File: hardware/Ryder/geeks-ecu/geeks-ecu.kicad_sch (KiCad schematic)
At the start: 25 parts, among them J101 7.62mm, J102 5.08mm, J103 JST XH, J104 5.08mm, J105 5.08mm, J106 5.08mm, J107 5.08mm, J108 5.08mm, J109 5.08mm, J110 5.08mm, J111 5.08mm, K101 J115F11A

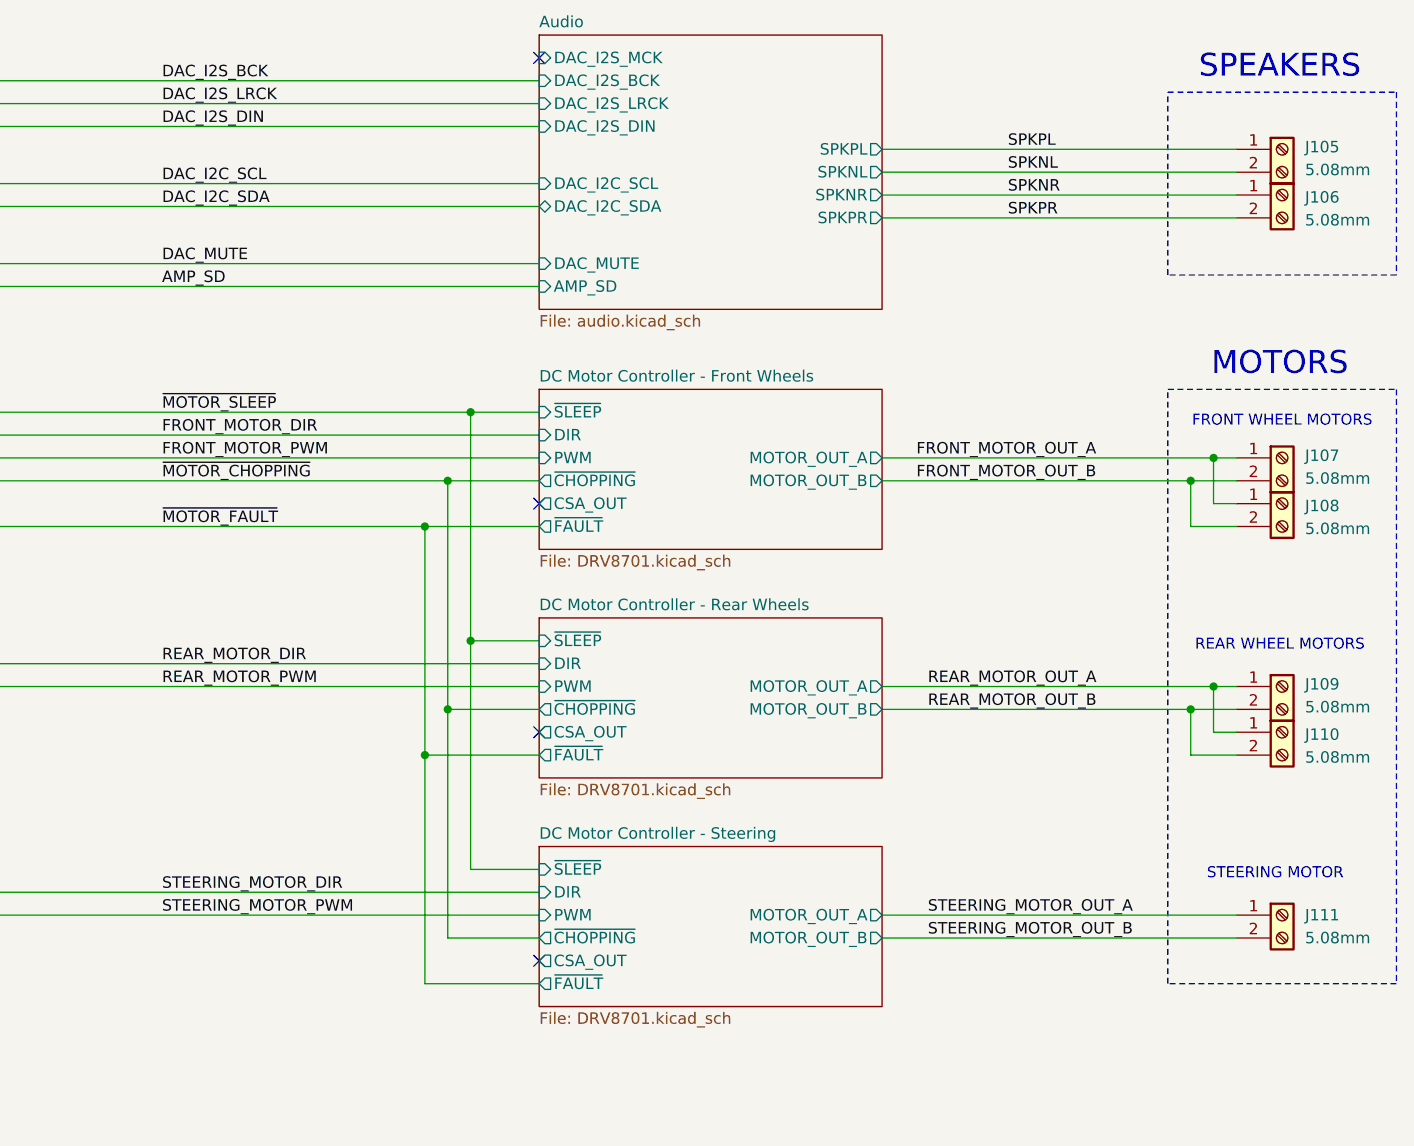
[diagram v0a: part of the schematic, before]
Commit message: Update Ryder ECU V1 Draft
Ryder ECU is close to completion, power planes and high current paths still need some work.
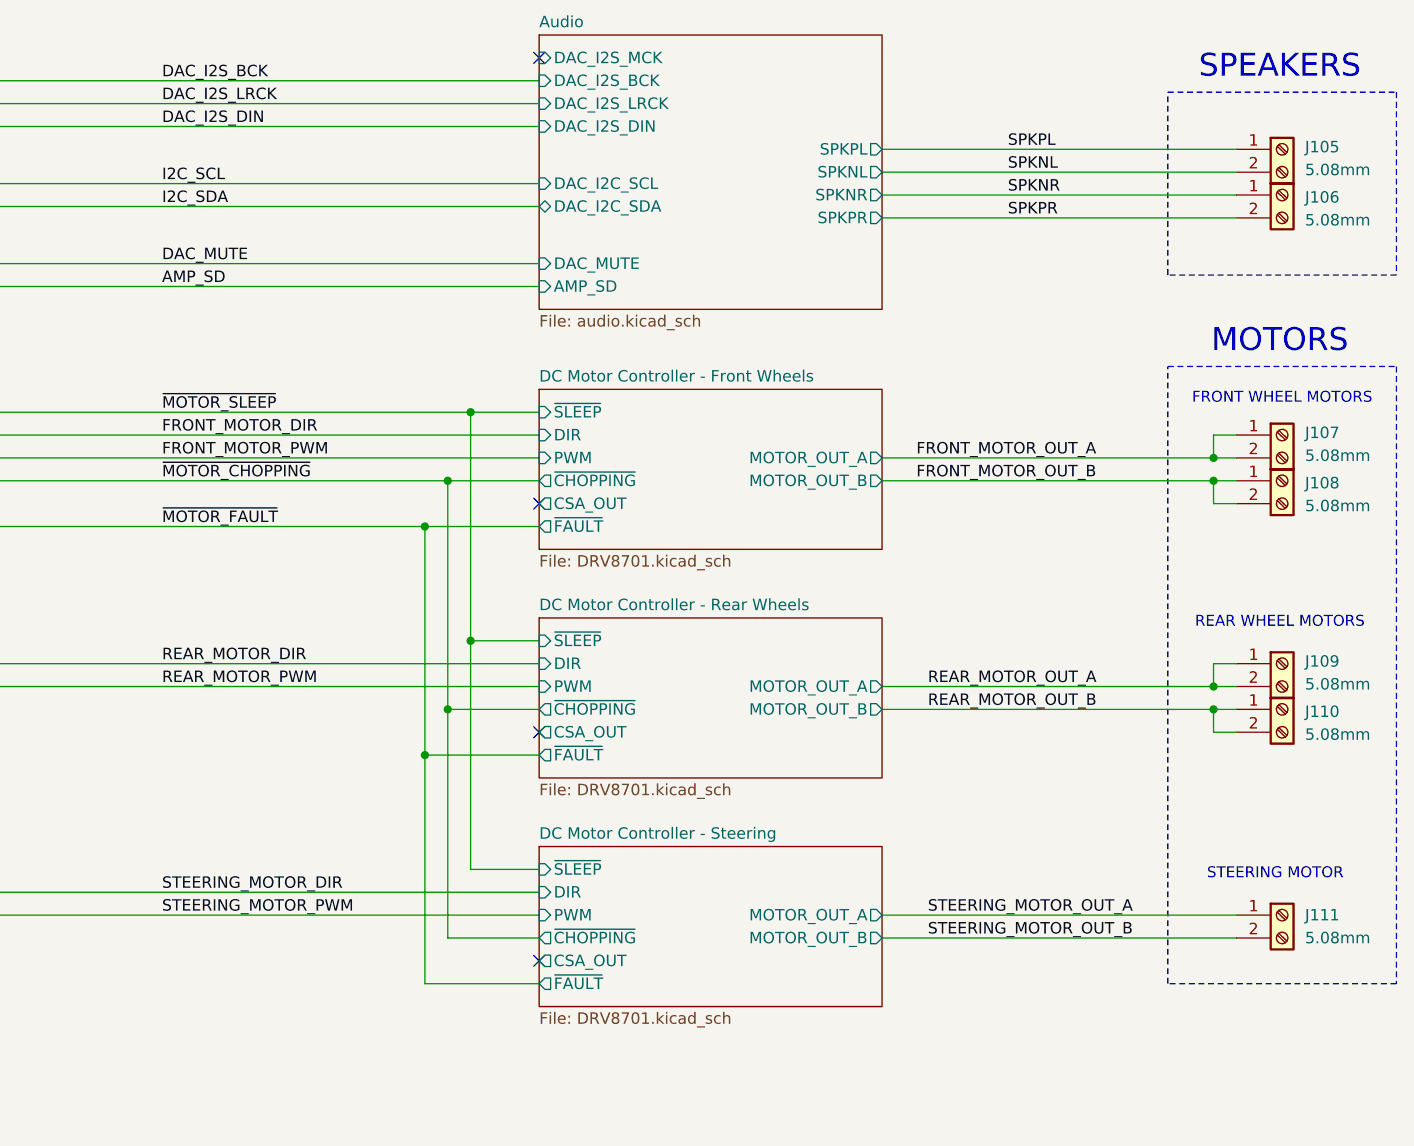
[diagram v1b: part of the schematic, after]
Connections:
- net FRONT_MOTOR_OUT_A: now also J107.2 (Pin_2); no longer J108.1 (Pin_1)
- net FRONT_MOTOR_OUT_B: now also J108.1 (Pin_1); no longer J107.2 (Pin_2)
- net REAR_MOTOR_OUT_A: now also J109.2 (Pin_2); no longer J110.1 (Pin_1)
- net REAR_MOTOR_OUT_B: now also J110.1 (Pin_1); no longer J109.2 (Pin_2)
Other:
- moved on the sheet: J107, J108, J109, J110

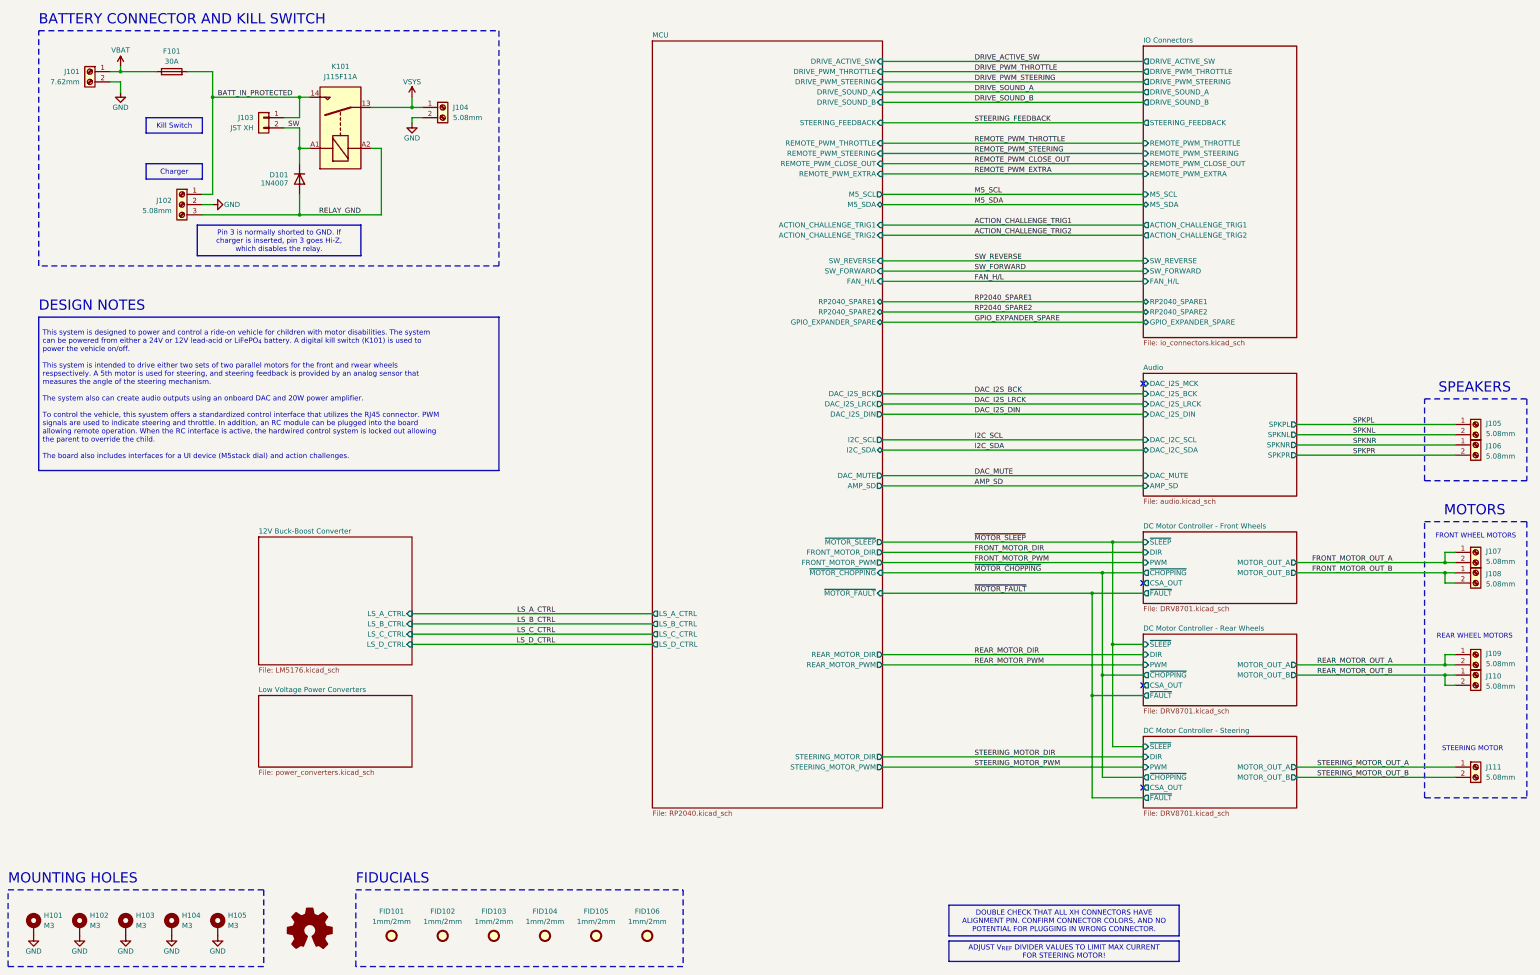
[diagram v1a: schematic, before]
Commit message: Ryder ECU Updates
Continuing to clean up ECU design
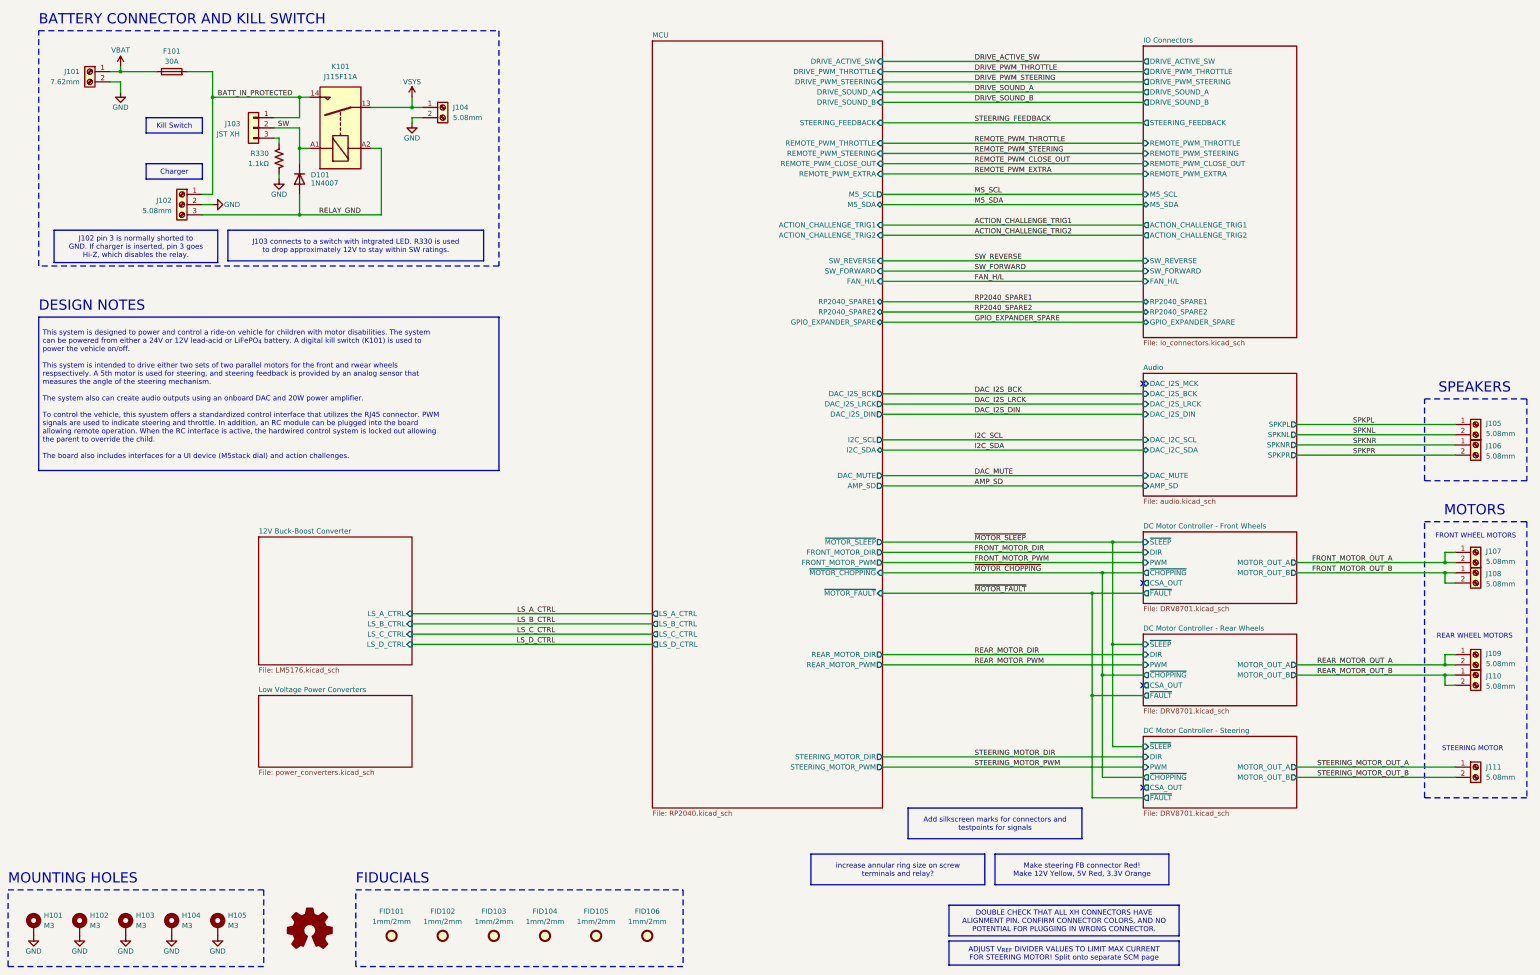
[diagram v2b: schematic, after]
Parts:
- removed J103: JST XH, geeks-ecu-footprints:JST_XH_B2B-XH-AM_1x02_P2.50mm_Vertical, symbol Connector_Generic:Conn_01x02
- added J103: JST XH, geeks-ecu-footprints:JST_XH_B3B-XH-AM_1x03_P2.50mm_Vertical, symbol Connector_Generic:Conn_01x03
- added R330: 1.1kΩ, Resistor_SMD:R_1206_3216Metric, symbol Device:R_US
- D101: footprint Diode_SMD:D_SOD-123F -> Diode_SMD:D_SOD-123; MPN C64898 -> C7420318
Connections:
- net BATT_IN_PROTECTED: now also J103.1 (Pin_1)
- net GND: now also R330.2
- net SW: now also J103.2 (Pin_2)
- new net: J103.3 (Pin_3), R330.1
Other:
- moved on the sheet: D101

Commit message: Ryder ECU Cleanup
Still need to work on high current traces
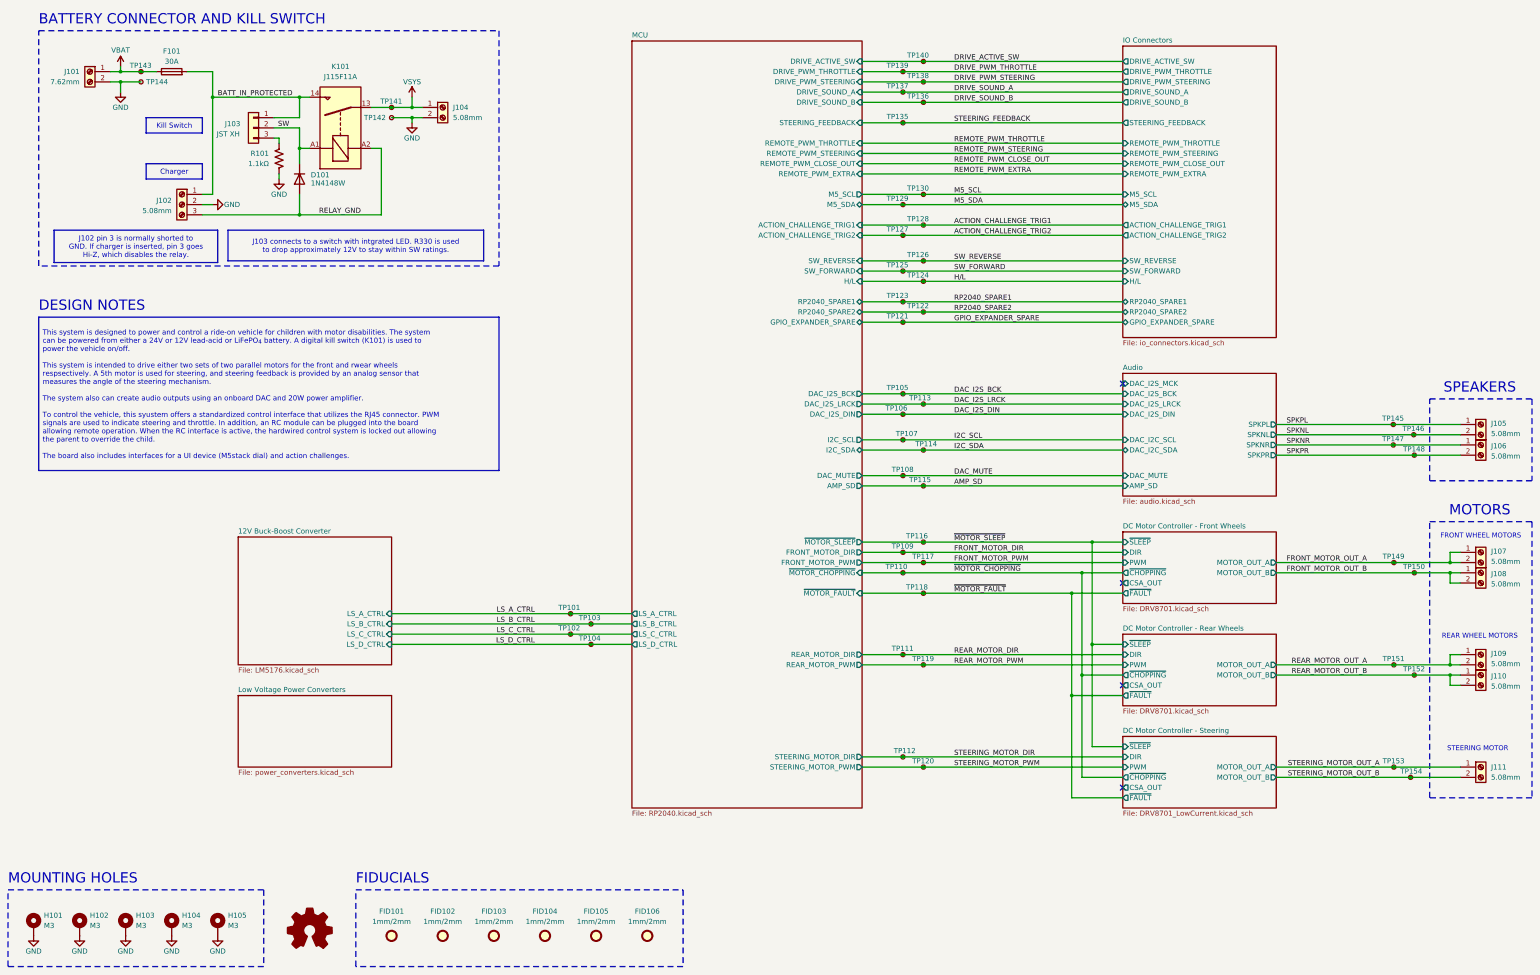
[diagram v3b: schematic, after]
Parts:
- added TP101, TP102, TP103, TP104, TP105, TP106, TP107, TP108, TP109, TP110, TP111, TP112, TP113, TP114, TP115, TP116, TP117, TP118, TP119, TP120, TP121, TP122, TP123, TP124, TP125, TP126, TP127, TP128, TP129, TP130, TP135, TP136, TP137, TP138, TP139, TP140, TP141, TP142, TP143, TP144, TP145, TP146, TP147, TP148, TP149, TP150, TP151, TP152, TP153, TP154: TestPoint_Small, geeks-ecu-footprints:TestPoint_Pad_D1.0mm, symbol Connector:TestPoint_Small
- D101: value 1N4007 -> 1N4148W; footprint Diode_SMD:D_SOD-123 -> geeks-ecu-footprints:D_SOD-123
- FID101, FID102, FID103, FID104, FID105, FID106: footprint Fiducial:Fiducial_1mm_Mask2mm -> geeks-ecu-footprints:Fiducial_1mm_Mask2mm
- H101, H102, H103, H104, H105: footprint MountingHole:MountingHole_3.2mm_M3_Pad_Via -> geeks-ecu-footprints:MountingHole_3.2mm_M3_Pad_Via
- J101: footprint geeks-ecu-footprints:TerminalBlock_CUI_TB007-508-02_1x02_P5.08mm_Horizontal -> geeks-ecu-footprints:TerminalBlock_CUI_TB005-762-02BE_1x02_P7.62mm_Horizontal
- R101: renamed from R330; footprint Resistor_SMD:R_1206_3216Metric -> geeks-ecu-footprints:R_1206_3216Metric
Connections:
- net ACTION_CHALLENGE_TRIG1: now also TP128.1
- net ACTION_CHALLENGE_TRIG2: now also TP127.1
- net AMP_SD: now also TP115.1
- net DAC_I2S_BCK: now also TP105.1
- net DAC_I2S_DIN: now also TP106.1
- net DAC_I2S_LRCK: now also TP113.1
- net DAC_MUTE: now also TP108.1
- net DRIVE_ACTIVE_SW: now also TP140.1
- net DRIVE_PWM_STEERING: now also TP138.1
- net DRIVE_PWM_THROTTLE: now also TP139.1
- net DRIVE_SOUND_A: now also TP137.1
- net DRIVE_SOUND_B: now also TP136.1
- net FRONT_MOTOR_DIR: now also TP109.1
- net FRONT_MOTOR_OUT_A: now also TP149.1
- net FRONT_MOTOR_OUT_B: now also TP150.1
- net FRONT_MOTOR_PWM: now also TP117.1
- net GND: now also TP142.1, TP144.1
- net GPIO_EXPANDER_SPARE: now also TP121.1
- net I2C_SCL: now also TP107.1
- net I2C_SDA: now also TP114.1
- net LS_A_CTRL: now also TP101.1
- net LS_B_CTRL: now also TP103.1
- net LS_C_CTRL: now also TP102.1
- net LS_D_CTRL: now also TP104.1
- net M5_SCL: now also TP130.1
- net M5_SDA: now also TP129.1
- net REAR_MOTOR_DIR: now also TP111.1
- net REAR_MOTOR_OUT_A: now also TP151.1
- net REAR_MOTOR_OUT_B: now also TP152.1
- net REAR_MOTOR_PWM: now also TP119.1
- net RP2040_SPARE1: now also TP123.1
- net RP2040_SPARE2: now also TP122.1
- net SPKNL: now also TP146.1
- net SPKNR: now also TP147.1
- net SPKPL: now also TP145.1
- net SPKPR: now also TP148.1
- net STEERING_FEEDBACK: now also TP135.1
- net STEERING_MOTOR_DIR: now also TP112.1
- net STEERING_MOTOR_OUT_A: now also TP153.1
- net STEERING_MOTOR_OUT_B: now also TP154.1
- net STEERING_MOTOR_PWM: now also TP120.1
- net SW_FORWARD: now also TP125.1
- net SW_REVERSE: now also TP126.1
- net VBAT: now also TP143.1
- net VSYS: now also TP141.1
- net ~{MOTOR_CHOPPING}: now also TP110.1
- net ~{MOTOR_FAULT}: now also TP118.1
- net ~{MOTOR_SLEEP}: now also TP116.1
- new net H/L: TP124.1
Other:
- sheet DC Motor Controller - Steering: file DRV8701.kicad_sch -> DRV8701_LowCurrent.kicad_sch
- sheet IO Connectors ports: added H/L; removed FAN_H/L
- sheet MCU ports: added H/L; removed FAN_H/L
- moved on the sheet: J105, J106, J107, J108, J109, J110, J111

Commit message: Finalize Ryder ECU
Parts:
- F101: MPN 3568 -> C5249699
- K101: now left out of the parts list

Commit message: Final Ryder ECU Design Files
All done!
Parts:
- J101, J102, J104, J105, J106, J107, J108, J109, J110, J111: now left out of the parts list
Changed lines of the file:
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@@
 		(body_style 1)
 		(exclude_from_sim no)
-		(in_bom yes)
+		(in_bom no)
 		(on_board yes)
-		(in_pos_files yes)
+		(in_pos_files no)
 		(dnp no)
 		(property "Reference" "J102"
@@
 		(in_bom no)
 		(on_board yes)
-		(in_pos_files yes)
+		(in_pos_files no)
 		(dnp no)
 		(fields_autoplaced yes)
@@
 		(body_style 1)
 		(exclude_from_sim no)
-		(in_bom yes)
+		(in_bom no)
 		(on_board yes)
-		(in_pos_files yes)
+		(in_pos_files no)
 		(dnp no)
 		(property "Reference" "J106"
@@
 		(in_bom no)
 		(on_board yes)
-		(in_pos_files yes)
+		(in_pos_files no)
 		(dnp no)
 		(fields_autoplaced yes)
@@
 		(body_style 1)
 		(exclude_from_sim no)
-		(in_bom yes)
+		(in_bom no)
 		(on_board yes)
-		(in_pos_files yes)
+		(in_pos_files no)
 		(dnp no)
 		(property "Reference" "J110"
@@
 		(body_style 1)
 		(exclude_from_sim no)
-		(in_bom yes)
+		(in_bom no)
 		(on_board yes)
-		(in_pos_files yes)
+		(in_pos_files no)
 		(dnp no)
 		(property "Reference" "J105"
@@
 		(in_bom no)
 		(on_board yes)
-		(in_pos_files yes)
+		(in_pos_files no)
 		(dnp no)
 		(fields_autoplaced yes)
@@
 		(body_style 1)
 		(exclude_from_sim no)
-		(in_bom yes)
+		(in_bom no)
 		(on_board yes)
-		(in_pos_files yes)
+		(in_pos_files no)
 		(dnp no)
 		(property "Reference" "J101"
@@
 		(in_bom no)
 		(on_board yes)
-		(in_pos_files yes)
+		(in_pos_files no)
 		(dnp no)
 		(fields_autoplaced yes)
@@
 		(body_style 1)
 		(exclude_from_sim no)
-		(in_bom yes)
+		(in_bom no)
 		(on_board yes)
-		(in_pos_files yes)
+		(in_pos_files no)
 		(dnp no)
 		(fields_autoplaced yes)
@@
 		(body_style 1)
 		(exclude_from_sim no)
-		(in_bom yes)
+		(in_bom no)
 		(on_board yes)
-		(in_pos_files yes)
+		(in_pos_files no)
 		(dnp no)
 		(property "Reference" "J108"
@@
 		(body_style 1)
 		(exclude_from_sim no)
-		(in_bom yes)
+		(in_bom no)
 		(on_board yes)
-		(in_pos_files yes)
+		(in_pos_files no)
 		(dnp no)
 		(fields_autoplaced yes)
@@
 		(body_style 1)
 		(exclude_from_sim no)
-		(in_bom yes)
+		(in_bom no)
 		(on_board yes)
-		(in_pos_files yes)
+		(in_pos_files no)
 		(dnp no)
 		(property "Reference" "J109"
@@
 		(in_bom no)
 		(on_board yes)
-		(in_pos_files yes)
+		(in_pos_files no)
 		(dnp no)
 		(fields_autoplaced yes)
@@
 		(body_style 1)
 		(exclude_from_sim no)
-		(in_bom yes)
+		(in_bom no)
 		(on_board yes)
-		(in_pos_files yes)
+		(in_pos_files no)
 		(dnp no)
 		(property "Reference" "J107"
